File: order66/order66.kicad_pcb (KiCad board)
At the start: 2 copper layers, 228.6 x 123 mm, 146 parts, among them J1 NICEVIEW, J2 Pouch Battery Connector, J3 swd connector, J6 millmax connector, SW1 AUX1, SW10 Z, SW11 AUX7, SW12 2, SW13 W, SW14 S, SW15 X, SW16 LALT, SW17 3, SW18 E, SW19 D, SW2 ESC, SW20 C, SW21 GUI, SW22 4, SW23 R, SW24 F, SW25 V, SW26 RAISE, SW27 5, SW28 T, SW29 G, SW3 TAB, SW30 B, SW31 LSPACE, SW32 AUX2, SW33 6, SW34 Y, SW35 H, SW36 N, SW37 RSPACE, SW38 AUX3, SW39 7, SW4 CAPSLCK, SW40 U, SW41 J, SW42 M, SW43 LOWER, SW44 AUX4, SW45 8, SW46 I, SW47 K, SW48 ,<, SW49 LEFT, SW5 LSHIFT, SW50 9, SW51 O, SW52 L, SW53 .>, SW54 DOWN, SW55 AUX5, SW56 0, SW57 P, SW58 ;:, SW59 /?, SW6 LCTRL, SW60 UP, SW61 AUX6, SW62 BACKSPACE, SW63 BACKSLACH, SW64 ENTER, SW65 RSHIFT, SW66 RIGHT, SW67 RST, SW68 ON/OFF, SW7 1, SW8 Q, SW9 A, U1 NiceNano

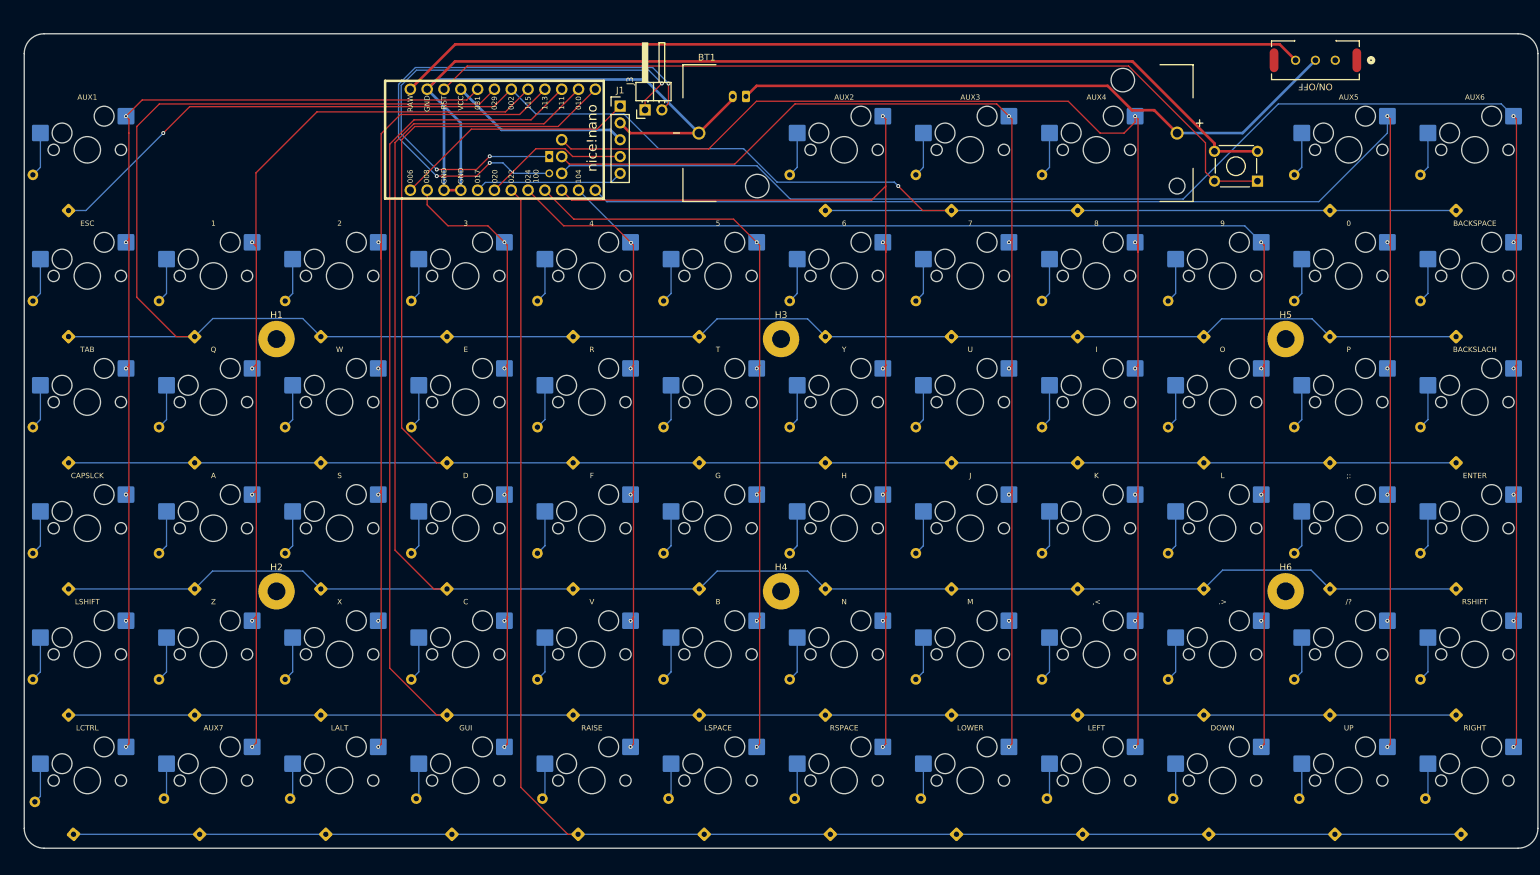
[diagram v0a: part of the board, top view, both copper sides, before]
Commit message: Trying smd and through hole diodes same time (#2)
* added the smd sod 123 package diode symbols. havent placed/routed all the footprints yet but seems to be okay. need to figure out what I want to do with the silkscreen references. probably should just place the base numbered one and dont use the other

* placed all diode footprints. need to sort out the silkscreen overlaps

* added the other version of power switch that I have as well just in case
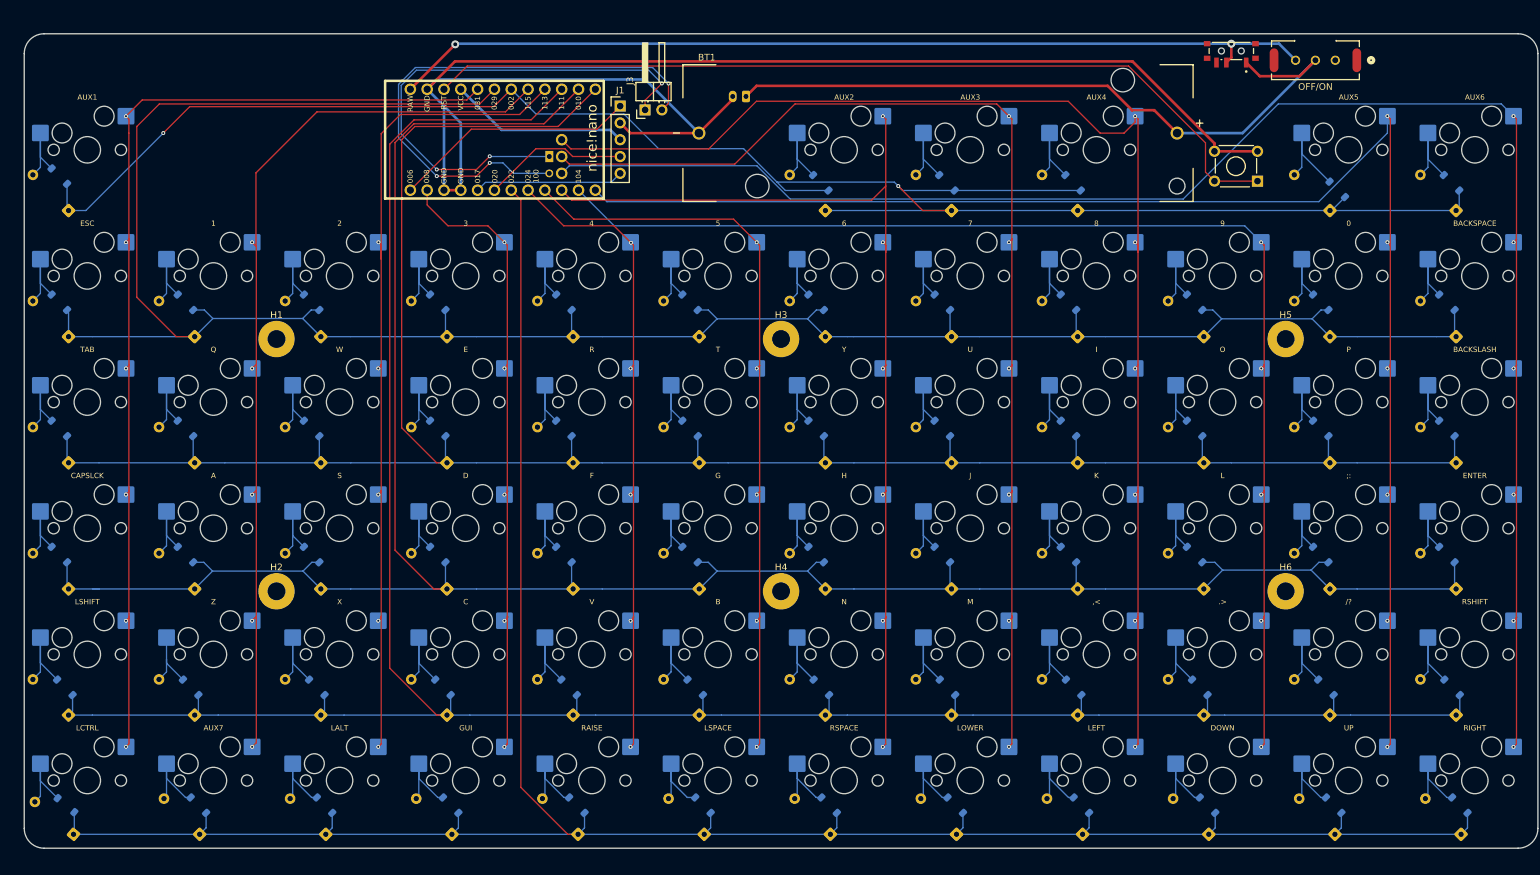
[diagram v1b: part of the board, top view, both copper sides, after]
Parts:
- added D101: 1N4148, Diode_SMD:D_SOD-123, B.Cu at (95.1, 85.0)
- added D102: 1N4148, Diode_SMD:D_SOD-123, B.Cu at (95.1, 104.0)
- added D103: 1N4148, Diode_SMD:D_SOD-123, B.Cu at (95.1, 123.1)
- added D104: 1N4148, Diode_SMD:D_SOD-123, B.Cu at (95.1, 142.2)
- added D105: 1N4148, Diode_SMD:D_SOD-123, B.Cu at (95.9, 162.2)
- added D106: 1N4148, Diode_SMD:D_SOD-123, B.Cu at (96.1, 180.0)
- added D107: 1N4148, Diode_SMD:D_SOD-123, B.Cu at (114.1, 104.0)
- added D108: 1N4148, Diode_SMD:D_SOD-123, B.Cu at (114.1, 123.1)
- added D109: 1N4148, Diode_SMD:D_SOD-123, B.Cu at (114.1, 142.2)
- added D110: 1N4148, Diode_SMD:D_SOD-123, B.Cu at (114.9, 162.2)
- added D111: 1N4148, Diode_SMD:D_SOD-123, B.Cu at (116.1, 180.0)
- added D112: 1N4148, Diode_SMD:D_SOD-123, B.Cu at (133.2, 104.0)
- added D113: 1N4148, Diode_SMD:D_SOD-123, B.Cu at (133.2, 123.1)
- added D114: 1N4148, Diode_SMD:D_SOD-123, B.Cu at (133.2, 142.2)
- added D115: 1N4148, Diode_SMD:D_SOD-123, B.Cu at (133.9, 162.2)
- added D116: 1N4148, Diode_SMD:D_SOD-123, B.Cu at (135.1, 180.0)
- added D117: 1N4148, Diode_SMD:D_SOD-123, B.Cu at (152.2, 104.0)
- added D118: 1N4148, Diode_SMD:D_SOD-123, B.Cu at (152.2, 123.1)
- added D119: 1N4148, Diode_SMD:D_SOD-123, B.Cu at (152.2, 142.2)
- added D120: 1N4148, Diode_SMD:D_SOD-123, B.Cu at (153.0, 162.2)
- added D121: 1N4148, Diode_SMD:D_SOD-123, B.Cu at (154.2, 180.0)
- added D122: 1N4148, Diode_SMD:D_SOD-123, B.Cu at (171.3, 104.0)
- added D123: 1N4148, Diode_SMD:D_SOD-123, B.Cu at (171.3, 123.1)
- added D124: 1N4148, Diode_SMD:D_SOD-123, B.Cu at (171.3, 142.2)
- added D125: 1N4148, Diode_SMD:D_SOD-123, B.Cu at (172.0, 162.2)
- added D126: 1N4148, Diode_SMD:D_SOD-123, B.Cu at (173.2, 180.0)
- added D127: 1N4148, Diode_SMD:D_SOD-123, B.Cu at (190.3, 104.0)
- added D128: 1N4148, Diode_SMD:D_SOD-123, B.Cu at (190.3, 123.1)
- added D129: 1N4148, Diode_SMD:D_SOD-123, B.Cu at (190.3, 142.2)
- added D130: 1N4148, Diode_SMD:D_SOD-123, B.Cu at (191.1, 162.2)
- added D131: 1N4148, Diode_SMD:D_SOD-123, B.Cu at (192.3, 180.0)
- added D132: 1N4148, Diode_SMD:D_SOD-123, B.Cu at (210.1, 86.0)
- added D133: 1N4148, Diode_SMD:D_SOD-123, B.Cu at (209.4, 104.0)
- added D134: 1N4148, Diode_SMD:D_SOD-123, B.Cu at (209.4, 123.1)
- added D135: 1N4148, Diode_SMD:D_SOD-123, B.Cu at (209.4, 142.2)
- added D136: 1N4148, Diode_SMD:D_SOD-123, B.Cu at (210.1, 162.2)
- added D137: 1N4148, Diode_SMD:D_SOD-123, B.Cu at (211.3, 180.0)
- added D138: 1N4148, Diode_SMD:D_SOD-123, B.Cu at (229.1, 86.0)
- added D139: 1N4148, Diode_SMD:D_SOD-123, B.Cu at (228.4, 104.0)
- added D140: 1N4148, Diode_SMD:D_SOD-123, B.Cu at (228.4, 123.1)
- added D141: 1N4148, Diode_SMD:D_SOD-123, B.Cu at (228.4, 142.2)
- added D142: 1N4148, Diode_SMD:D_SOD-123, B.Cu at (229.2, 162.2)
- added D143: 1N4148, Diode_SMD:D_SOD-123, B.Cu at (230.4, 180.0)
- added D144: 1N4148, Diode_SMD:D_SOD-123, B.Cu at (248.2, 86.0)
- added D145: 1N4148, Diode_SMD:D_SOD-123, B.Cu at (247.5, 104.0)
- added D146: 1N4148, Diode_SMD:D_SOD-123, B.Cu at (247.5, 123.1)
- added D147: 1N4148, Diode_SMD:D_SOD-123, B.Cu at (247.5, 142.2)
- added D148: 1N4148, Diode_SMD:D_SOD-123, B.Cu at (248.2, 162.2)
- added D149: 1N4148, Diode_SMD:D_SOD-123, B.Cu at (249.4, 180.0)
- added D150: 1N4148, Diode_SMD:D_SOD-123, B.Cu at (266.5, 104.0)
- added D151: 1N4148, Diode_SMD:D_SOD-123, B.Cu at (266.5, 123.1)
- added D152: 1N4148, Diode_SMD:D_SOD-123, B.Cu at (266.5, 142.2)
- added D153: 1N4148, Diode_SMD:D_SOD-123, B.Cu at (267.3, 162.2)
- added D154: 1N4148, Diode_SMD:D_SOD-123, B.Cu at (268.5, 180.0)
- added D155: 1N4148, Diode_SMD:D_SOD-123, B.Cu at (288.1, 87.0)
- added D156: 1N4148, Diode_SMD:D_SOD-123, B.Cu at (285.6, 104.0)
- added D157: 1N4148, Diode_SMD:D_SOD-123, B.Cu at (285.6, 123.1)
- added D158: 1N4148, Diode_SMD:D_SOD-123, B.Cu at (285.6, 142.2)
- added D159: 1N4148, Diode_SMD:D_SOD-123, B.Cu at (286.3, 162.2)
- added D160: 1N4148, Diode_SMD:D_SOD-123, B.Cu at (287.5, 180.0)
- added D161: 1N4148, Diode_SMD:D_SOD-123, B.Cu at (305.3, 86.0)
- added D162: 1N4148, Diode_SMD:D_SOD-123, B.Cu at (304.6, 104.0)
- added D163: 1N4148, Diode_SMD:D_SOD-123, B.Cu at (304.6, 123.1)
- added D164: 1N4148, Diode_SMD:D_SOD-123, B.Cu at (304.6, 142.2)
- added D165: 1N4148, Diode_SMD:D_SOD-123, B.Cu at (305.4, 162.2)
- added D166: 1N4148, Diode_SMD:D_SOD-123, B.Cu at (306.6, 180.0)
- added SW100: OFF/ON, SSSS811101:SW_SSSS811101, F.Cu at (272.1, 66.1)
- SW63: value BACKSLACH -> BACKSLASH
- SW68: value ON/OFF -> OFF/ON
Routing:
- net ROW2: track 294.5 -> 344.0 mm
- net ROW0: track 244.0 -> 290.6 mm
- net ROW3: track 319.2 -> 364.4 mm
- net ROW1: track 309.6 -> 354.2 mm
- net ROW5: track 311.9 -> 355.3 mm
- net ROW4: track 329.7 -> 369.3 mm
- net BATT+: track 94.3 -> 106.6 mm
- net Net-(D155-A): track 6.79 -> 15.9 mm
- net Net-(D105-A): track 6.79 -> 14.2 mm
- net Net-(D159-A): track 6.79 -> 14.2 mm
- net Net-(D153-A): track 6.79 -> 14.2 mm
- net Net-(D148-A): track 6.79 -> 14.2 mm
- net Net-(D136-A): track 6.79 -> 14.2 mm
- net Net-(D130-A): track 6.79 -> 14.2 mm
- net Net-(D125-A): track 6.79 -> 14.2 mm
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
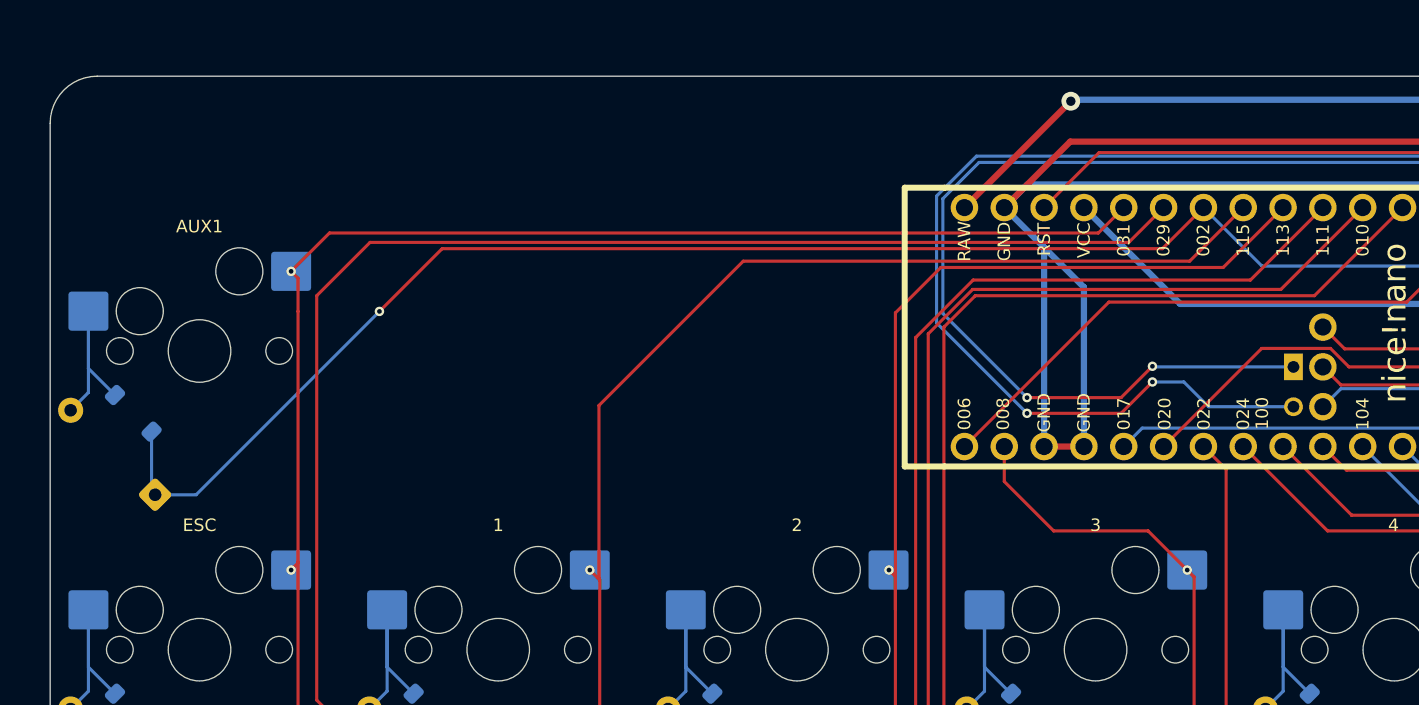
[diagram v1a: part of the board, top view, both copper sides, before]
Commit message: adding both an order 66 logo and a connector for the jlink but that needs work
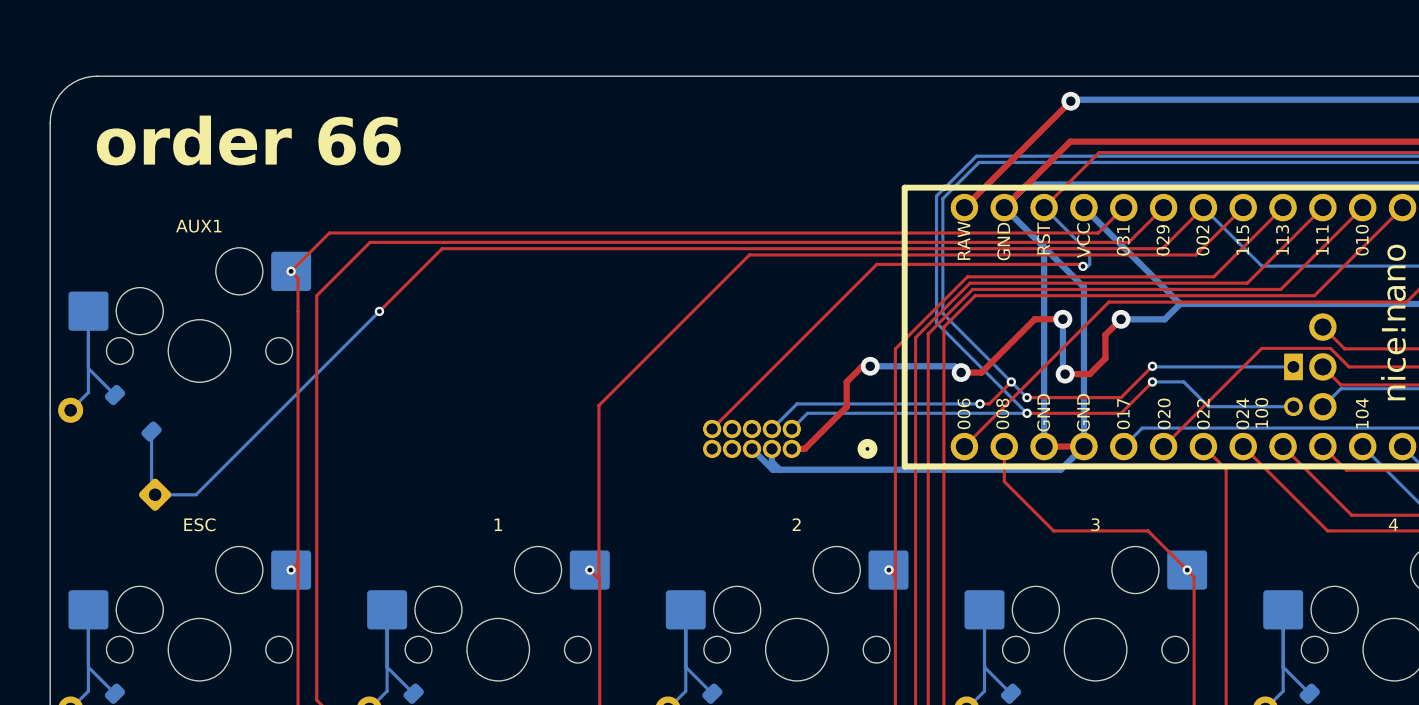
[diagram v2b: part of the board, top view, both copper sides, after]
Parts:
- added J4: 3220-10-0100-00, 3220_10_0100_00:CONN_3220-10-0100-00_CNC, B.Cu at (137.1, 87.3)
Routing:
- net VCC: track 27.2 -> 62.8 mm, vias 0 -> 5
- net RST: track 134.1 -> 167.5 mm, vias 0 -> 1
- net GND: track 231.5 -> 255.3 mm
- net SWC: track 79.0 -> 95.5 mm, vias 3 -> 5
- net SWD: track 82.0 -> 97.4 mm
- net COL2: track 126.0 -> 124.7 mm
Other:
- board text added: "order 66"

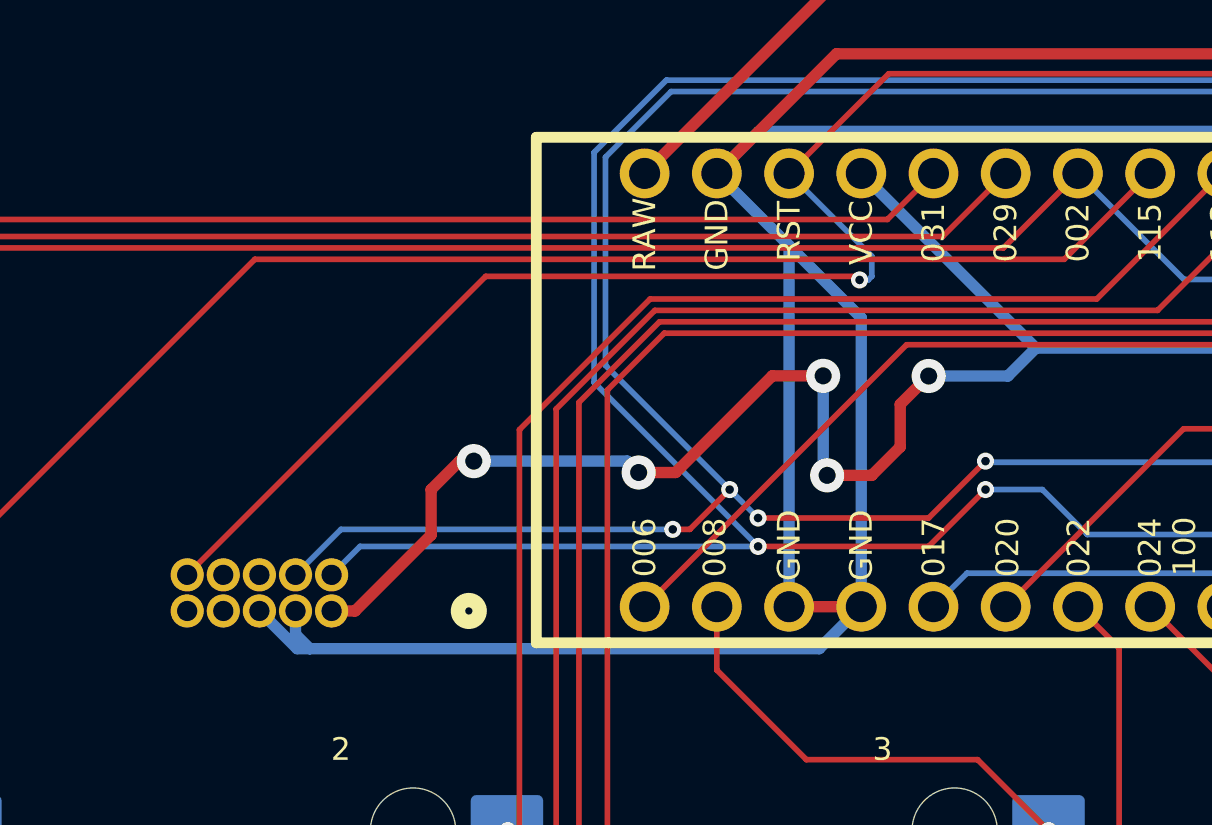
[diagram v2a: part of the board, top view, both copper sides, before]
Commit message: removing the connector for the link for now
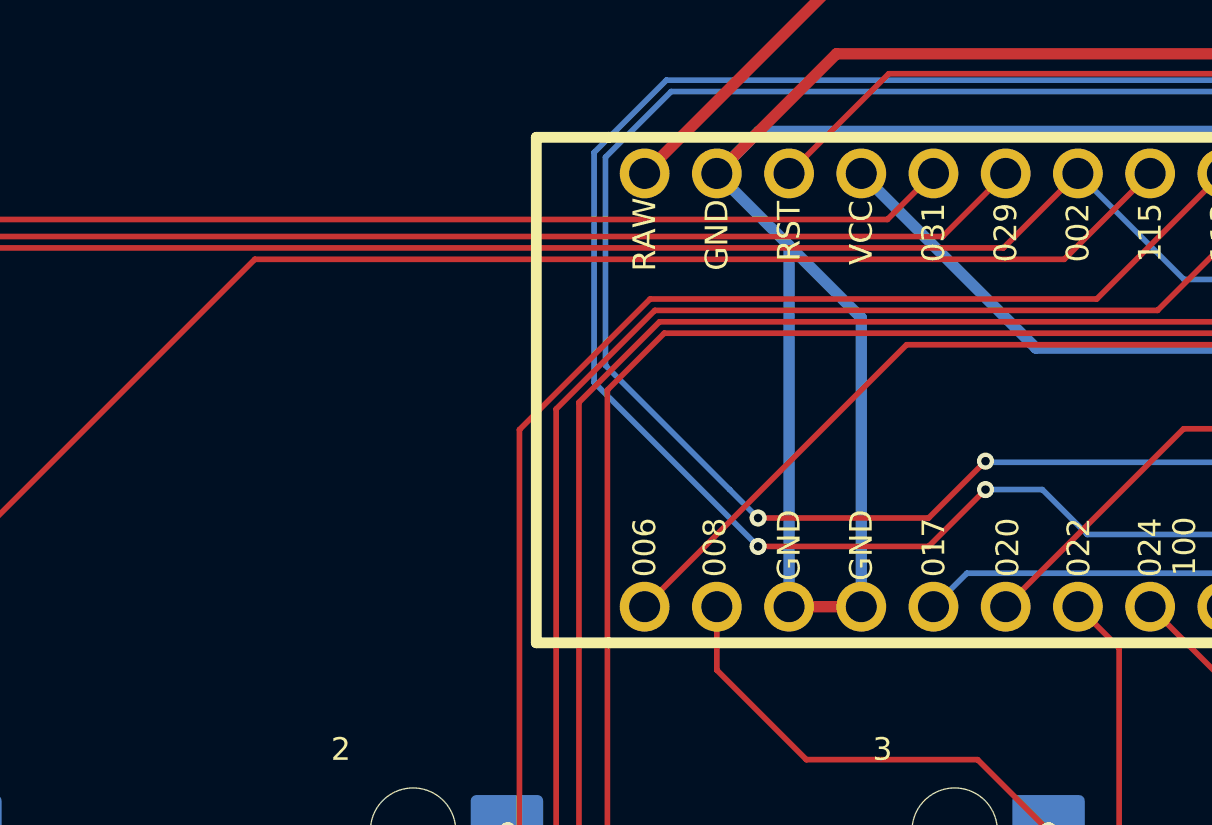
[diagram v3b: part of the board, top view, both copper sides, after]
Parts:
- removed J4: 3220-10-0100-00, 3220_10_0100_00:CONN_3220-10-0100-00_CNC
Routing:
- net VCC: track 62.8 -> 27.2 mm, vias 5 -> 0
- net RST: track 167.5 -> 134.1 mm, vias 1 -> 0
- net GND: track 255.3 -> 231.5 mm
- net SWC: track 95.5 -> 79.0 mm, vias 5 -> 3
- net SWD: track 97.4 -> 82.0 mm
